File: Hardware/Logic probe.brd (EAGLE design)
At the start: 111.4 x 12.7 mm, 19 parts, among them IC1 74HC00, J1 GND_connector, Q1 BC847B

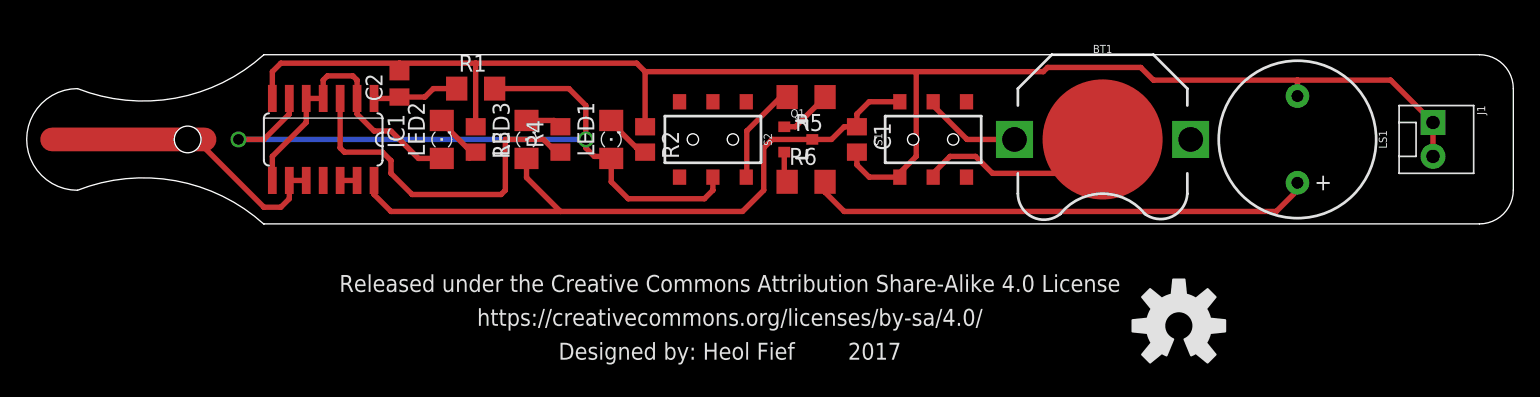
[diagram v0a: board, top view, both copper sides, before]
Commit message: Add files via upload
Fix buzzer circuit
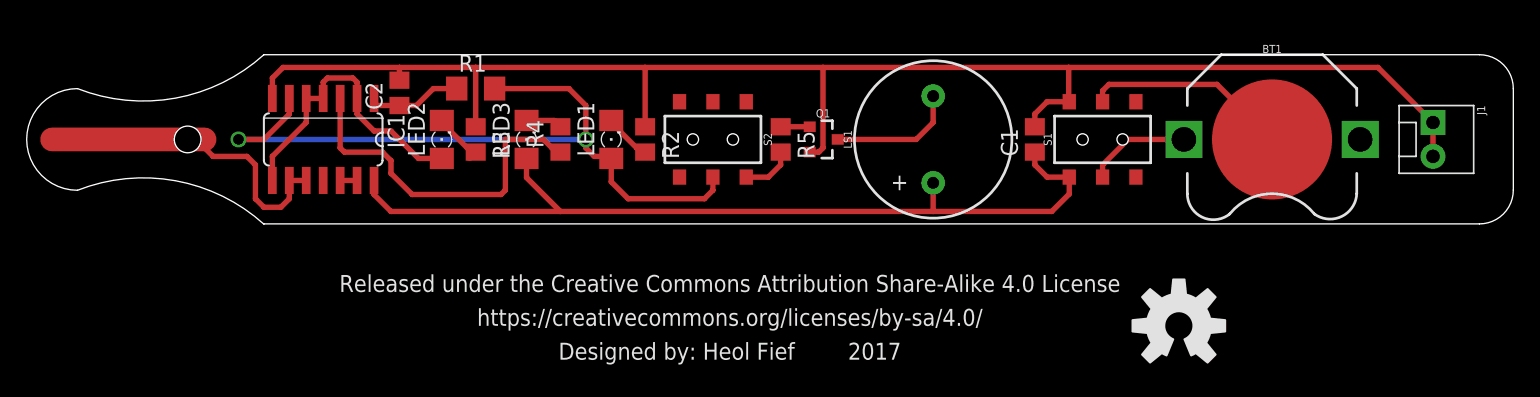
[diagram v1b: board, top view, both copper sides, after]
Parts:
- removed R6: 330, resistor:R1206
- R1: value 50k -> 47k
- R5: device resistor:R1206 -> resistor:R0805
- moved LS1 27.3 mm to (66.7, 6.35), turned to 90 degrees
- moved C1 13.3 mm to (74.3, 6.35), turned to 90 degrees
- moved BT1 12.7 mm to (92.1, 6.35)
- moved S1 12.7 mm to (79.4, 6.35)
- moved R5 3.70 mm to (55.2, 6.35), turned to 270 degrees
- moved Q1 1.91 mm to (58.4, 6.35)
- moved C2 0.63 mm to (26.7, 9.84)
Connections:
- removed net N$11: BT1.VCC@1, S1.2
- net GND: now also Q1.2, S1.1; no longer LS1.-, S1.4
- net N$12: now also BT1.VCC@1; no longer BT1.GND
- net N$5: now also LS1.+, Q1.3; no longer Q1.2, R6.1
- net N$6: now also BT1.GND, S1.2; no longer LS1.+, R6.2
- net VCC: now also LS1.-, S1.4; no longer Q1.3, S1.1
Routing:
- net N$6: track 38.0 -> 15.4 mm
- net VCC: track 52.6 -> 67.3 mm
- net N$12: track 16.6 -> 7.81 mm
- net N$11: track 7.43 -> 0.00 mm
- net N$5: track 2.31 -> 9.66 mm
- net N$2: track 7.55 -> 3.92 mm
- net N$4: track 3.98 -> 2.18 mm
- net PROBE: track 23.2 -> 24.6 mm
- net GND: track 117.6 -> 116.6 mm
- net N$7: track 6.48 -> 7.26 mm

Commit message: Add files via upload
Change battery size & probe lenght
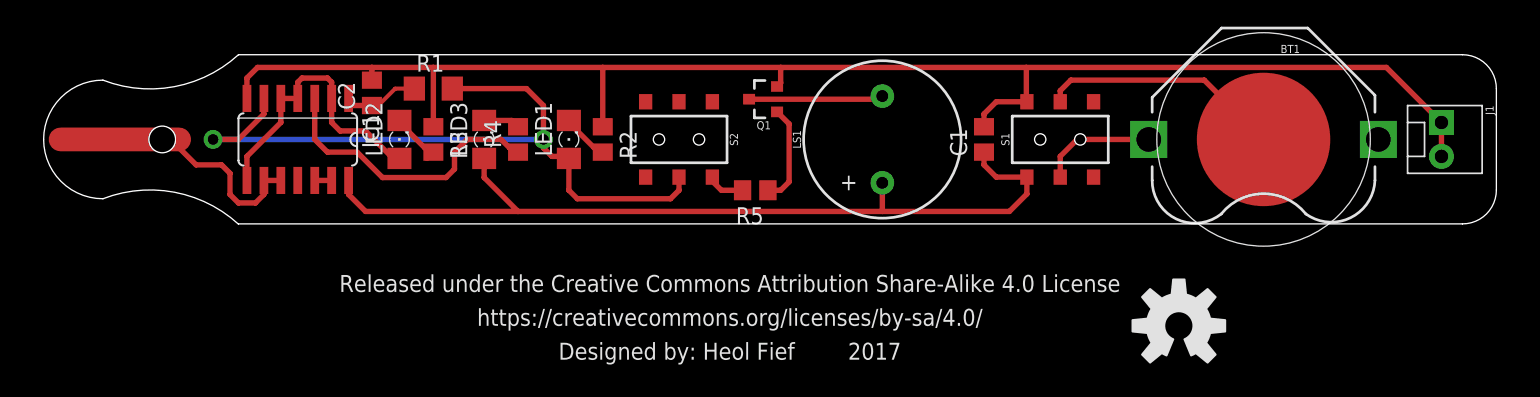
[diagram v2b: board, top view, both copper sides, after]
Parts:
- BT1: device SparkFun-Batteries:BATTCON_12MM_PTH -> SparkFun-Batteries:BATTCON_16MM_PTH
- moved Q1 5.37 mm to (54.0, 9.37), turned to 90 degrees
- moved R5 4.26 mm to (53.3, 2.54), turned to 180 degrees
- moved C1 3.81 mm to (70.5, 6.35)
- moved LS1 3.81 mm to (62.9, 6.35)
- moved LED1 3.18 mm to (39.4, 6.35)
- moved R2 3.18 mm to (41.9, 6.35)
- moved LED2 3.17 mm to (26.7, 6.35)
- moved LED3 3.17 mm to (33.0, 6.35)
- moved R1 3.17 mm to (29.2, 10.2)
- moved R3 3.17 mm to (29.2, 6.35)
- moved R4 3.17 mm to (35.6, 6.35)
- moved S1 3.17 mm to (76.2, 6.35)
- moved S2 2.54 mm to (47.6, 6.35)
- moved C2 2.06 mm to (24.6, 9.84)
- moved IC1 1.90 mm to (19.1, 6.35)
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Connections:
- net N$12: now also BT1.VCC@2
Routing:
- net N$4: track 2.18 -> 7.47 mm
- net N$9: track 26.6 -> 21.8 mm
- net PROBE: track 24.6 -> 21.1 mm
- net N$6: track 15.4 -> 18.2 mm
- net GND: track 116.6 -> 114.2 mm
- net N$7: track 7.26 -> 5.99 mm
- net N$2: track 3.92 -> 2.85 mm
- net N$12: track 7.81 -> 8.72 mm
- net N$3: track 22.6 -> 21.7 mm
- net VCC: track 67.3 -> 66.7 mm
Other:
- board size 111.4 x 12.7 mm -> 108.9 x 12.7 mm
